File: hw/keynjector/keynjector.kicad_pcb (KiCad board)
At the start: 2 copper layers, 36 x 42.7 mm, 44 parts, among them J1 10118192-0001LF, J2 M50-3600542, J3 FH12A-40S-0.5SH(55), J4 492250821, SW1 EVQ-P7L01P, U1 PRTR5V0U2X, U2 SPX3819M5-L/TR, U3 ATSAM4S8BA-ANR, U4 ADS7843

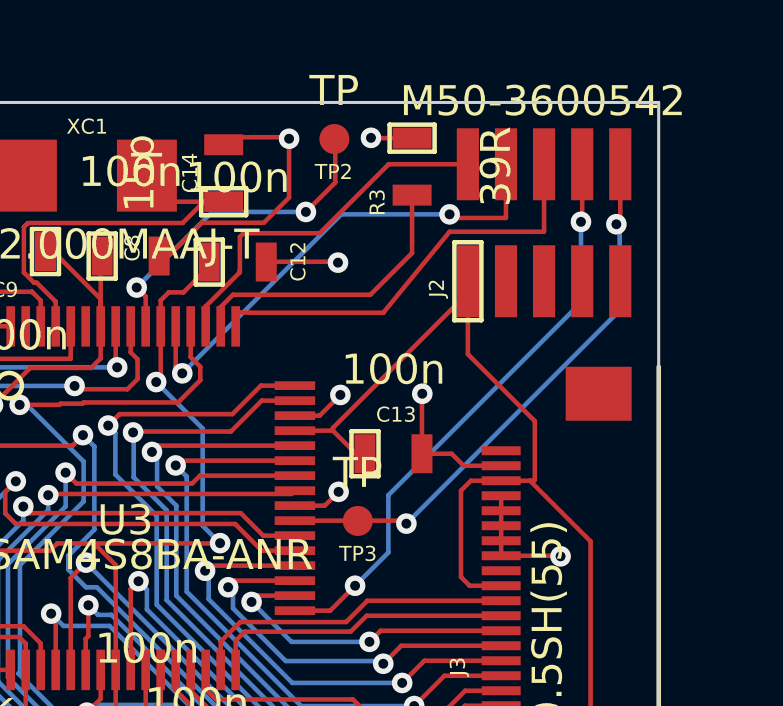
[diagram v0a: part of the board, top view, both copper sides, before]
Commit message: moved debug header to board back to facilitate debug with board in case
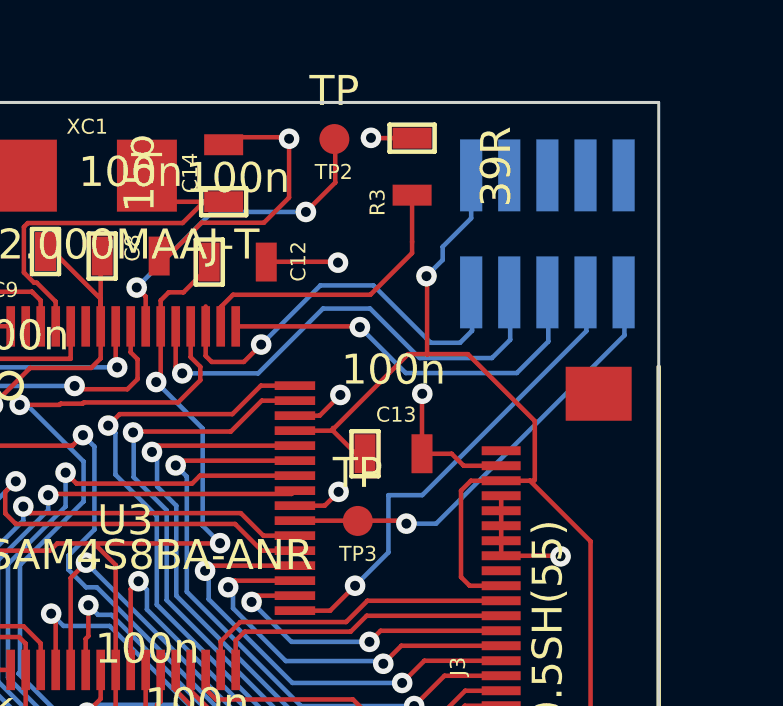
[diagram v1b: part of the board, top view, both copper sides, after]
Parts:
- J2: moved to B.Cu
- moved J2 6.07 mm to (92.2, 67.2)
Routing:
- net /keynjector_debug/NRST: track 18.8 -> 15.6 mm, vias 2 -> 1
- net /keynjector_debug/TDI: track 19.5 -> 16.5 mm, vias 2 -> 1
- net VCC_MCU_P3V3: track 189.2 -> 192.2 mm, vias 4 -> 5
- net /keynjector_debug/TMS: track 12.1 -> 14.5 mm, vias 0 -> 1
- net /keynjector_debug/TDO: track 14.3 -> 14.2 mm, vias 0 -> 1
- net /keynjector_debug/TCK: vias 2 -> 1

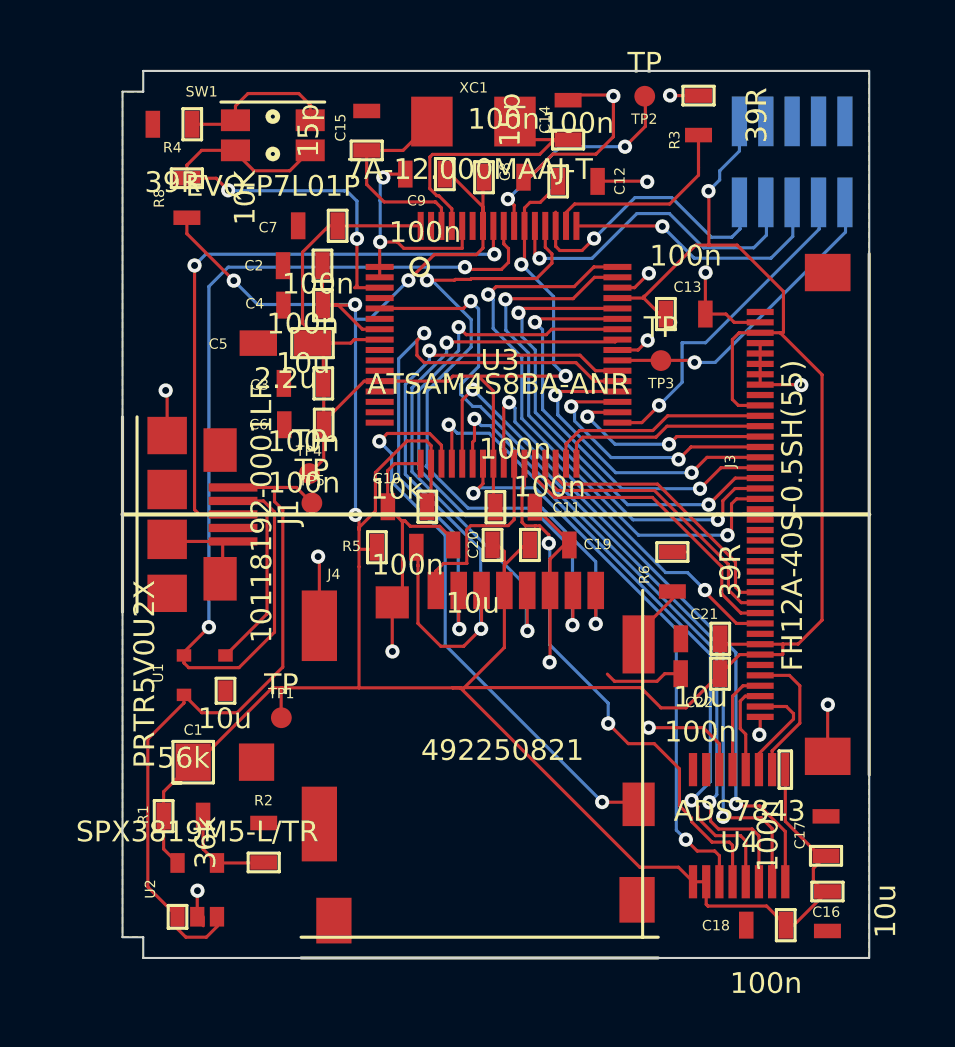
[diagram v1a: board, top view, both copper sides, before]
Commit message: moved erase testpoint to back to facilitate debugging/reprogramming in debug case adjusted version number on PCB to 1.0.0 for first real release
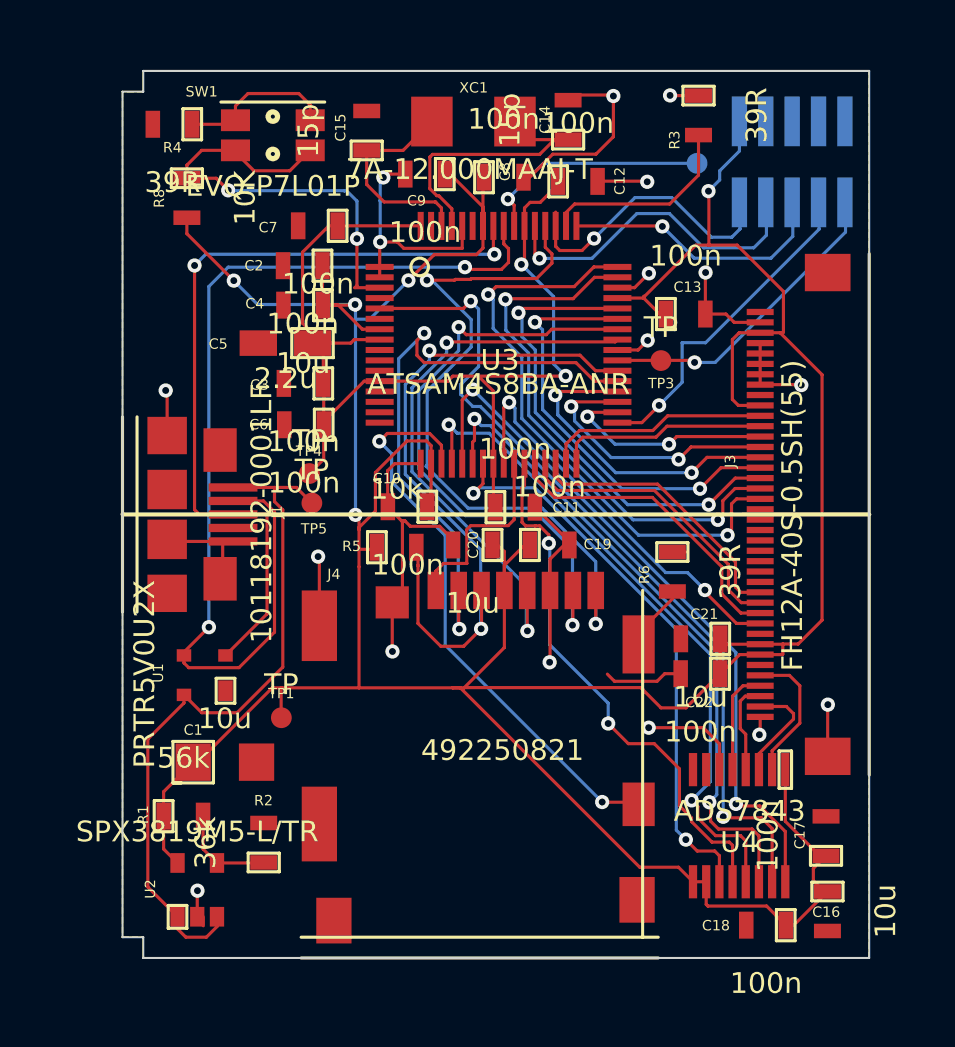
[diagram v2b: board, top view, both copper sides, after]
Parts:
- TP2: moved to B.Cu
- moved TP2 4.10 mm to (87.7, 64.5)
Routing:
- net /keynjector_mcu/ERASE: track 10.8 -> 11.2 mm, vias 2 -> 1
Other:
- board text added: "ERASE"
- board text added: "keynjector 1.0.0 © Jonas Hagmar 2014"
- board text removed: "keynjector 1.1.0 © Jonas Hagmar 2014"
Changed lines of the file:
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@@
     (area 55.594823 58.8926 183.014286 104.6674)
     (thickness 1.6)
-    (drawings 12)
-    (tracks 798)
+    (drawings 13)
+    (tracks 796)
     (zones 0)
     (modules 44)
@@
   (module TP (layer F.Cu)
     (at 69.12 80.81)
-    (fp_text reference TP5 (at 0 -1.08) (layer F.SilkS)
+    (fp_text reference TP5 (at 0.1 1.24) (layer F.SilkS)
       (effects (font (size 0.5 0.5) (thickness 0.125)))
     )
@@
     )
   )
-  (module TP (layer F.Cu)
-    (at 85.15 61.22)
-    (fp_text reference TP2 (at -0.02 1.1) (layer F.SilkS)
-      (effects (font (size 0.5 0.5) (thickness 0.125)))
-    )
-    (fp_text value TP (at 0 -1.6) (layer F.SilkS)
-      (effects (font (size 1 1) (thickness 0.15)))
+  (module TP (layer B.Cu)
+    (at 87.67 64.45)
+    (fp_text reference TP2 (at -0.02 -1.1) (layer B.SilkS)
+      (effects (font (size 0.5 0.5) (thickness 0.125)) (justify mirror))
+    )
+    (fp_text value TP (at 0 1.6) (layer B.SilkS)
+      (effects (font (size 1 1) (thickness 0.15)) (justify mirror))
     )
     (pad 1 smd circle (at 0 0) (size 1 1)
-      (layers F.Cu F.Paste F.Mask)
+      (layers B.Cu B.Paste B.Mask)
       (net 29 /keynjector_mcu/ERASE)
     )
@@
   (module 10118192 (layer F.Cu)
     (at 62.15 81.36 270)
-    (fp_text reference J1 (at -0.1 -5.85 270) (layer F.SilkS)
-      (effects (font (size 1 1) (thickness 0.15)))
+    (fp_text reference J1 (at -0.12 -5.29 270) (layer F.SilkS)
+      (effects (font (size 0.5 0.5) (thickness 0.125)))
     )
     (fp_text value 10118192-0001LF (at -0.05 -4.55 270) (layer F.SilkS)
@@
       (net 42 GND)
     )
+  )
+  (gr_text ERASE (at 87.53 65.56) (layer B.SilkS)
+    (effects (font (size 0.5 0.5) (thickness 0.125)) (justify mirror))
   )
   (gr_text "Copyright 2014 Jonas Hagmar\n\nThis file is part of keynjector.\n\nkeynjector is free software: you can redistribute it and/or modify\nit under the terms of the GNU General Public License as published by\nthe Free Software Foundation, either version 2 of the License, or\n(at your option) any later version.\n\nkeynjector is distributed in the hope that it will be useful,\nbut WITHOUT ANY WARRANTY; without even the implied warranty of\nMERCHANTABILITY or FITNESS FOR A PARTICULAR PURPOSE.  See the\nGNU General Public License for more details.\n\nYou should have received a copy of the GNU General Public License\nalong with keynjector.  If not, see <http://www.gnu.org/licenses/>" (at 142.15 60.63) (layer Cmts.User)
@@
   (gr_line (start 61 101.72) (end 60 101.72) (angle 90) (layer Edge.Cuts) (width 0.1))
   (gr_line (start 61 102.72) (end 61 101.72) (angle 90) (layer Edge.Cuts) (width 0.1))
-  (gr_text "keynjector 1.1.0\n© Jonas Hagmar 2014" (at 78.01 97.01) (layer B.SilkS)
+  (gr_text "keynjector 1.0.0\n© Jonas Hagmar 2014" (at 78.01 97.01) (layer B.SilkS)
     (effects (font (size 1.5 1.5) (thickness 0.3)) (justify mirror))
   )
@@
   (segment (start 80.954802 80.204802) (end 85.614802 80.204802) (width 0.1524) (layer F.Cu) (net 28))
   (segment (start 80.36 79.61) (end 80.954802 80.204802) (width 0.1524) (layer F.Cu) (net 28))
+  (segment (start 78.56 66.17) (end 78.56 66.16) (width 0.1524) (layer B.Cu) (net 29))
+  (segment (start 78.86 66.47) (end 78.56 66.17) (width 0.1524) (layer F.Cu) (net 29))
+  (via (at 78.56 66.17) (size 0.6858) (layers F.Cu B.Cu) (net 29))
   (segment (start 78.86 67.465) (end 78.86 66.47) (width 0.1524) (layer F.Cu) (net 29) (status 10))
-  (segment (start 85.18 62.67) (end 85.18 61.38) (width 0.1524) (layer F.Cu) (net 29) (status 20))
-  (segment (start 84.2 63.65) (end 85.18 62.67) (width 0.1524) (layer F.Cu) (net 29))
-  (via (at 84.2 63.65) (size 0.6858) (layers F.Cu B.Cu) (net 29))
-  (segment (start 81.08 63.65) (end 84.2 63.65) (width 0.1524) (layer B.Cu) (net 29))
-  (segment (start 78.56 66.17) (end 81.08 63.65) (width 0.1524) (layer B.Cu) (net 29))
-  (via (at 78.56 66.17) (size 0.6858) (layers F.Cu B.Cu) (net 29))
-  (segment (start 78.86 66.47) (end 78.56 66.17) (width 0.1524) (layer F.Cu) (net 29))
+  (segment (start 80.27 64.45) (end 87.67 64.45) (width 0.1524) (layer B.Cu) (net 29))
+  (segment (start 78.56 66.16) (end 80.27 64.45) (width 0.1524) (layer B.Cu) (net 29))
   (segment (start 75.36 78.915) (end 75.36 78.03) (width 0.1524) (layer F.Cu) (net 30) (status 10))
   (via (at 72.37 77.84) (size 0.6858) (layers F.Cu B.Cu) (net 30))

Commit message: changed edge cuts to accomodate for screen support
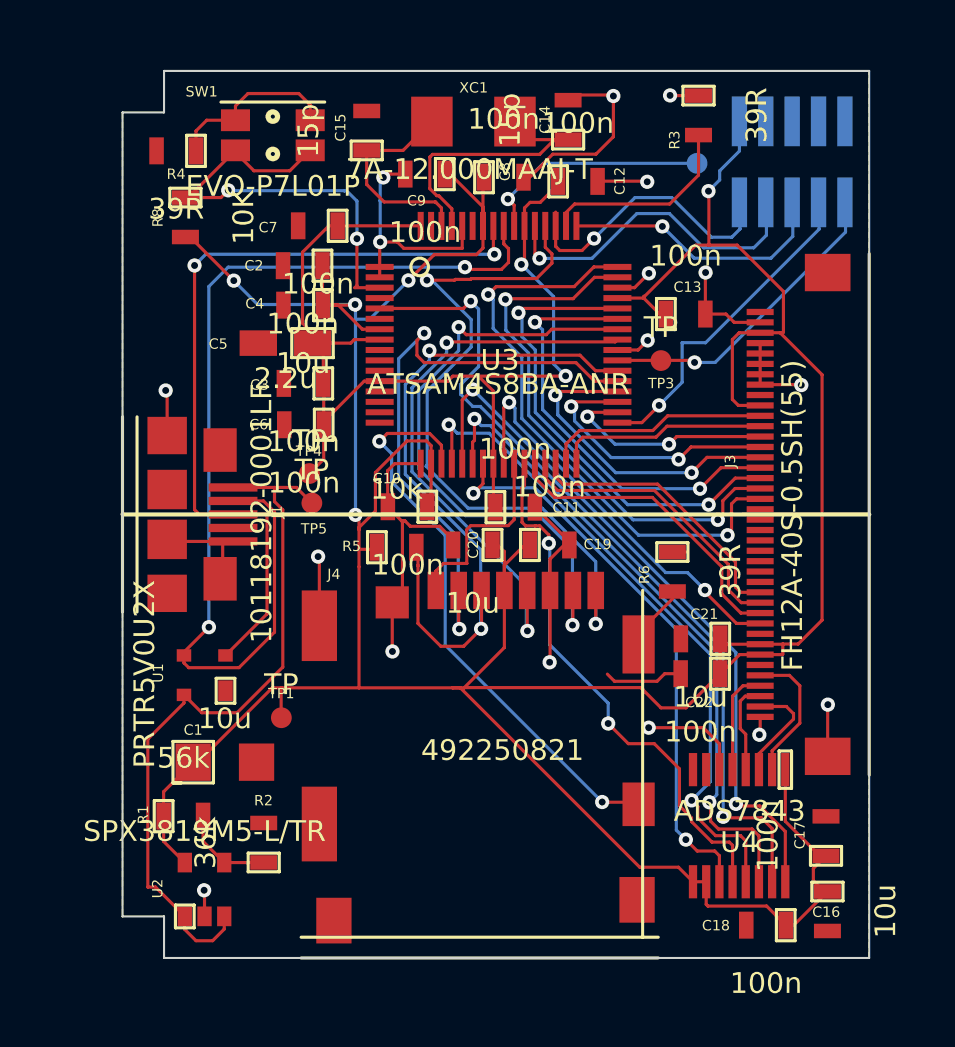
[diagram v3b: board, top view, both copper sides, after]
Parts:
- moved R4 1.29 mm to (62.6, 63.9)
- moved R8 0.93 mm to (63.0, 67.0)
- moved U2 0.35 mm to (64.0, 99.4)
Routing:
- net N-0000053: track 7.66 -> 8.85 mm
- net VCC_MCU_P3V3: track 192.2 -> 191.6 mm
- net VCC_USB_P5V0: track 34.3 -> 34.9 mm
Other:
- outline, holes or cut-outs redrawn
